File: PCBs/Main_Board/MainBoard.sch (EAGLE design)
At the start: 24 parts

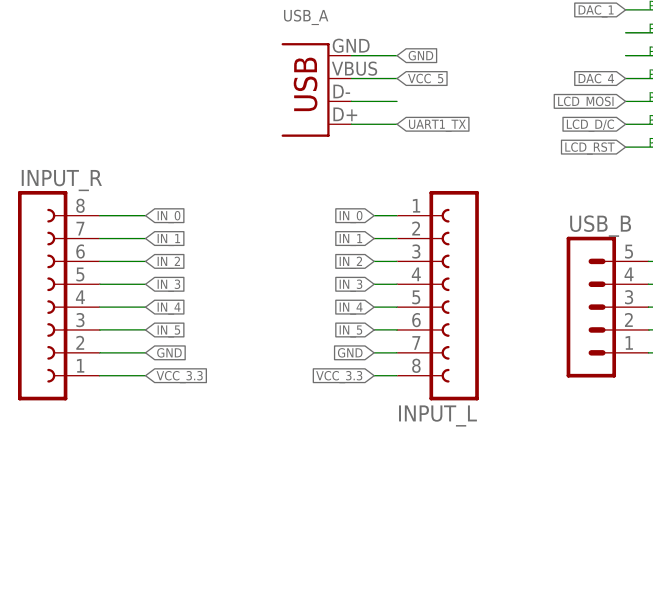
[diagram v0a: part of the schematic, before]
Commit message: Created main board layout
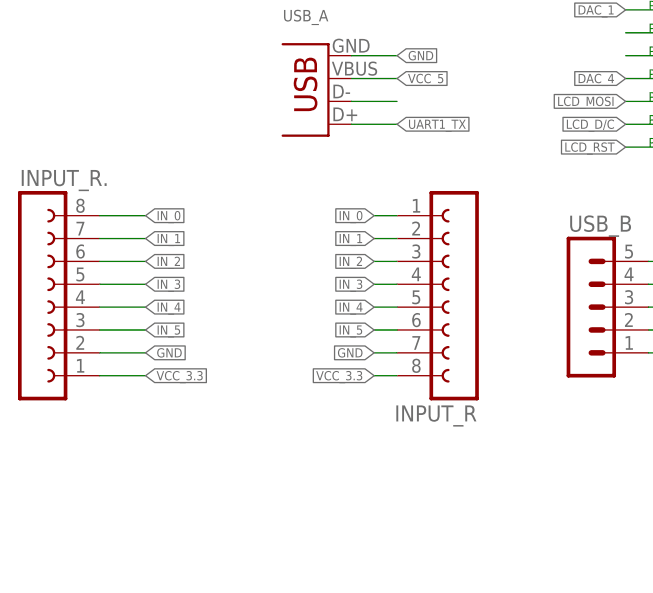
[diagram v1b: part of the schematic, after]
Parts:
- removed INPUT_L: (no value), con-lsta:FE08W
- added INPUT_R.: (no value), con-lsta:FE08W
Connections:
- net GND: now also INPUT_R..2, INPUT_R.7; no longer INPUT_L.7, INPUT_R.2
- net IN_0: now also INPUT_R..8, INPUT_R.1; no longer INPUT_L.1, INPUT_R.8
- net IN_1: now also INPUT_R..7, INPUT_R.2; no longer INPUT_L.2, INPUT_R.7
- net IN_2: now also INPUT_R..6, INPUT_R.3; no longer INPUT_L.3, INPUT_R.6
- net IN_3: now also INPUT_R..5, INPUT_R.4; no longer INPUT_L.4, INPUT_R.5
- net IN_4: now also INPUT_R..4, INPUT_R.5; no longer INPUT_L.5, INPUT_R.4
- net IN_5: now also INPUT_R..3, INPUT_R.6; no longer INPUT_L.6, INPUT_R.3
- net VCC_3.3: now also INPUT_R..1, INPUT_R.8; no longer INPUT_L.8, INPUT_R.1
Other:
- moved on the sheet: INPUT_R
